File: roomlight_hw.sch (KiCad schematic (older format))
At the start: 56 parts, among them J1 24V_Conn, J2 LOADs, J3 UART2, J4 DATAs, J5 Touch_SW, J6 SWD, U1 INA180A, U2 STM32F103CBTx, U3 ESP-07, U4 MIC4690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

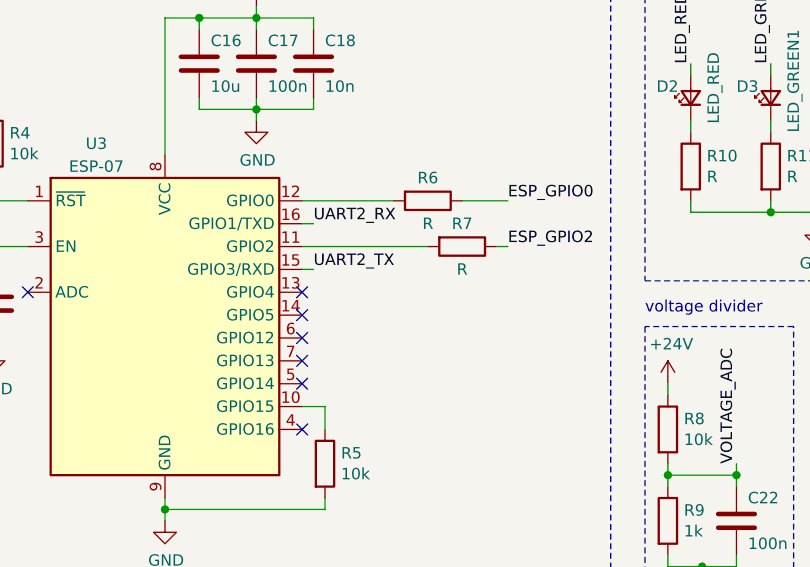
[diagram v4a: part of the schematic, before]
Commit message: Improve UART connection and a lot of ground planes
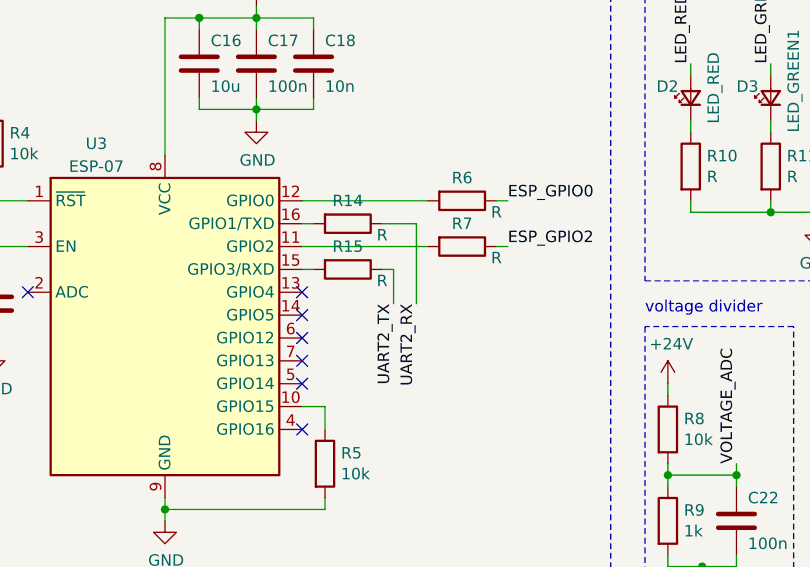
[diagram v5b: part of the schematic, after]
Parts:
- added R14, R15: R, Resistor_SMD:R_0603_1608Metric_Pad1.05x0.95mm_HandSolder, symbol Device:R
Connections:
- net UART2_RX: now also R14.1; no longer U3.16 (GPIO1/TXD)
- net UART2_TX: now also R15.1; no longer U3.15 (GPIO3/RXD)
- new net: R15.2, U3.15 (GPIO3/RXD)
- new net: R14.2, U3.16 (GPIO1/TXD)
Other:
- moved on the sheet: R6
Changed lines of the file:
@@
 L Device:R R6
 U 1 1 5F27210A
-P 6900 1800
-F 0 "R6" V 6800 1800 50  0000 C CNN
-F 1 "R" V 7000 1800 50  0000 C CNN
-F 2 "Resistor_SMD:R_0603_1608Metric_Pad1.05x0.95mm_HandSolder" V 6830 1800 50  0001 C CNN
-F 3 "~" H 6900 1800 50  0001 C CNN
-	1    6900 1800
+P 7050 1800
+F 0 "R6" V 6950 1800 50  0000 C CNN
+F 1 "R" V 7100 1950 50  0000 C CNN
+F 2 "Resistor_SMD:R_0603_1608Metric_Pad1.05x0.95mm_HandSolder" V 6980 1800 50  0001 C CNN
+F 3 "~" H 7050 1800 50  0001 C CNN
+	1    7050 1800
 	0    1    1    0
 $EndComp
@@
 P 7050 2000
 F 0 "R7" V 6950 2000 50  0000 C CNN
-F 1 "R" V 7150 2000 50  0000 C CNN
+F 1 "R" V 7100 2150 50  0000 C CNN
 F 2 "Resistor_SMD:R_0603_1608Metric_Pad1.05x0.95mm_HandSolder" V 6980 2000 50  0001 C CNN
 F 3 "~" H 7050 2000 50  0001 C CNN
@@
 	6900 2000 6350 2000
 Wire Wire Line
-	6350 1800 6750 1800
+	6350 1800 6900 1800
 Wire Wire Line
 	7200 2000 7250 2000
 Wire Wire Line
-	7050 1800 7250 1800
+	7200 1800 7250 1800
 Text Label 7250 1800 0    50   ~ 0
 ESP_GPIO0
@@
 Text Label 3600 3450 0    50   ~ 0
 UART2_RX
-Text Label 6400 1900 0    50   ~ 0
+Text Label 6850 2250 3    50   ~ 0
 UART2_RX
-Text Label 6400 2100 0    50   ~ 0
+Text Label 6750 2250 3    50   ~ 0
 UART2_TX
 Text Label 2200 3850 2    50   ~ 0
@@
 	3100 5450 3100 5600
 Connection ~ 3100 5600
+$Comp
+L Device:R R15
+U 1 1 5F3D0049
+P 6550 2100
+F 0 "R15" V 6450 2100 50  0000 C CNN
+F 1 "R" V 6600 2250 50  0000 C CNN
+F 2 "Resistor_SMD:R_0603_1608Metric_Pad1.05x0.95mm_HandSolder" V 6480 2100 50  0001 C CNN
+F 3 "~" H 6550 2100 50  0001 C CNN
+	1    6550 2100
+	0    1    1    0
+$EndComp
+$Comp
+L Device:R R14
+U 1 1 5F3D03AD
+P 6550 1900
+F 0 "R14" V 6450 1900 50  0000 C CNN
+F 1 "R" V 6600 2050 50  0000 C CNN
+F 2 "Resistor_SMD:R_0603_1608Metric_Pad1.05x0.95mm_HandSolder" V 6480 1900 50  0001 C CNN
+F 3 "~" H 6550 1900 50  0001 C CNN
+	1    6550 1900
+	0    1    1    0
+$EndComp
+Wire Wire Line
+	6750 2250 6750 2100
+Wire Wire Line
+	6750 2100 6700 2100
+Wire Wire Line
+	6700 1900 6850 1900
+Wire Wire Line
+	6850 1900 6850 2250
 $EndSCHEMATC
